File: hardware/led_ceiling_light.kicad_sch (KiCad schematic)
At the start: 22 parts

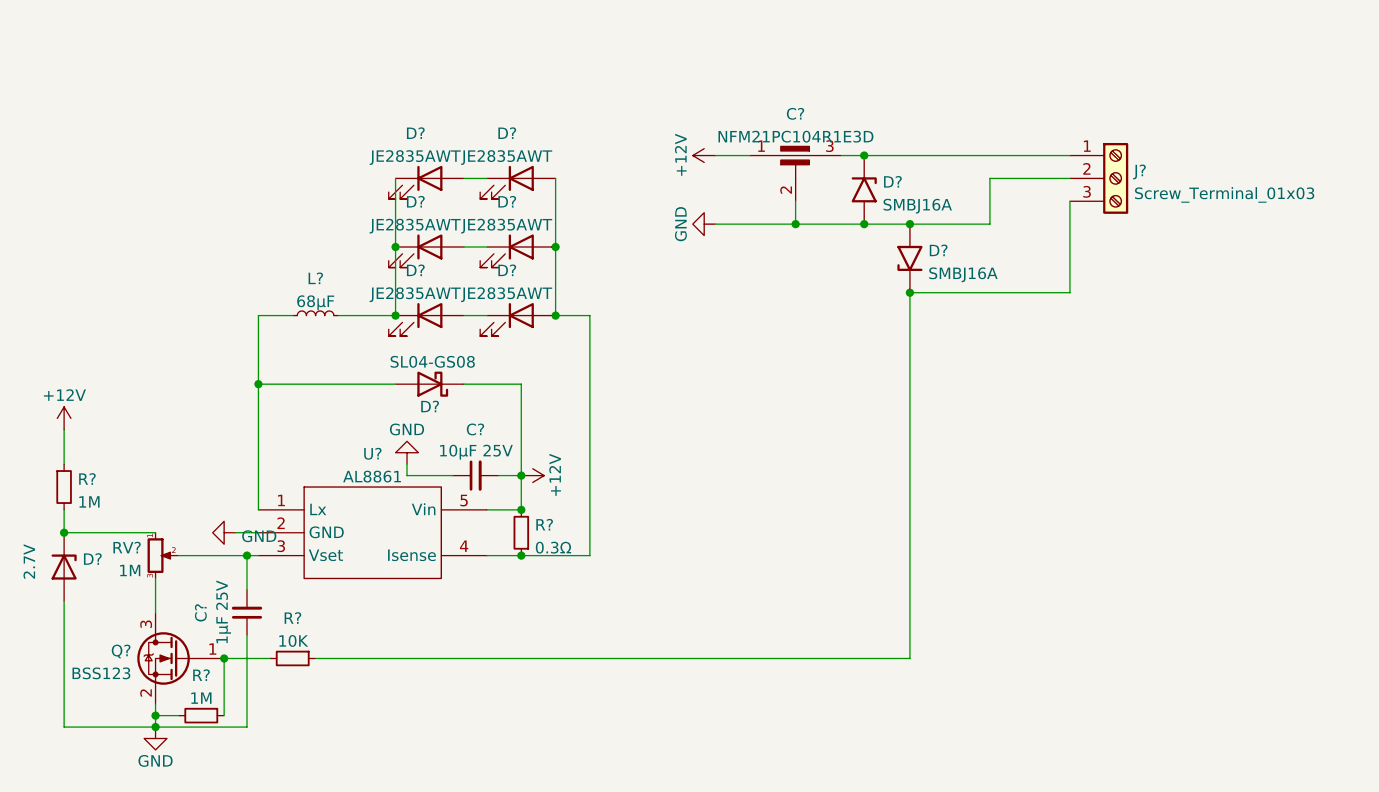
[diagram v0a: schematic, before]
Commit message: Fix some DRC issues; add more footprints.
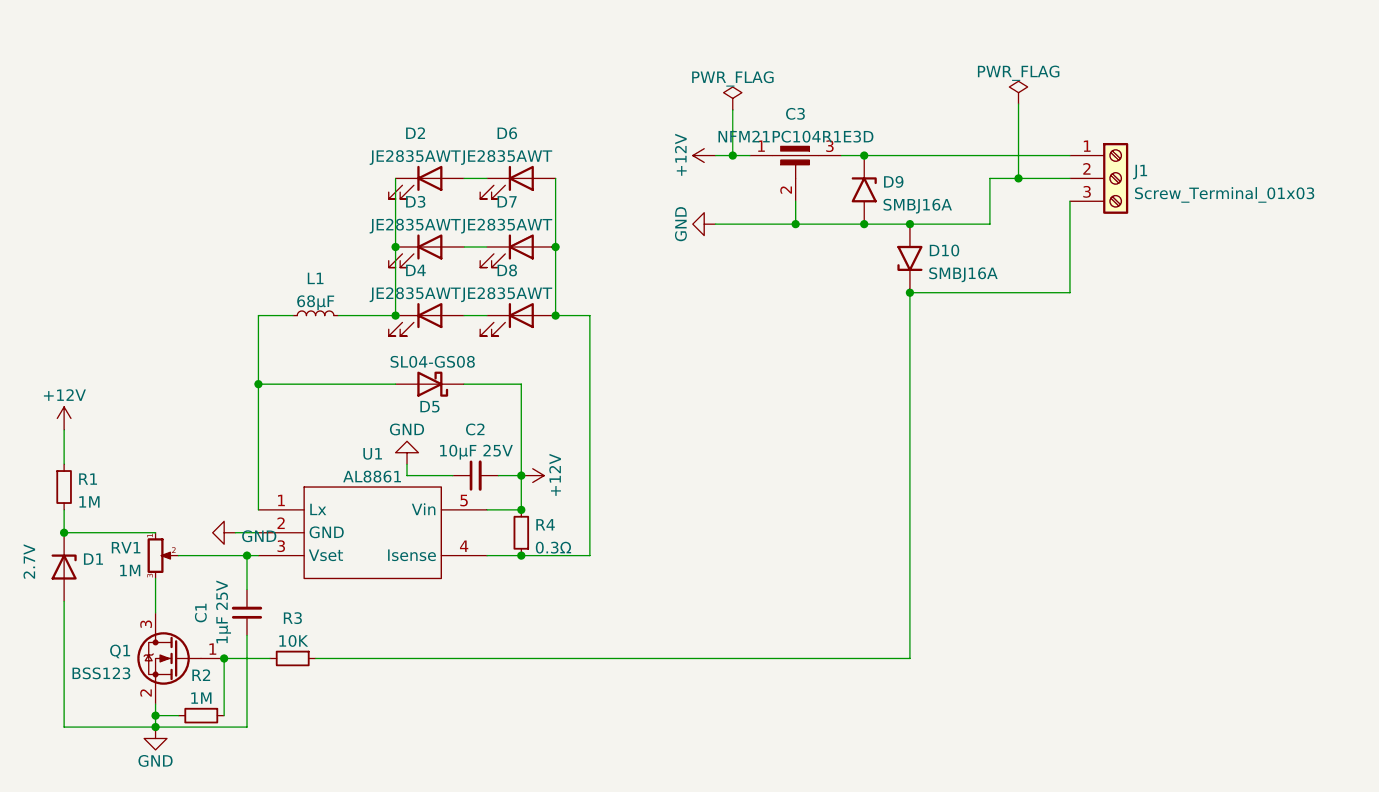
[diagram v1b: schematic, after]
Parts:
- Q1: renamed from Q?; footprint (none) -> Package_TO_SOT_SMD:SOT-23
- gave numbers to parts that had none: 21

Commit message: More part numbers and footprint
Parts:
- R1: footprint Resistor_SMD:R_0805_2012Metric_Pad1.20x1.40mm_HandSolder -> Resistor_SMD:R_2512_6332Metric_Pad1.40x3.35mm_HandSolder; P/N (none) -> WW25WR300FTL
- RV1: footprint (none) -> Potentiometer_THT:Potentiometer_Piher_PT-10-V10_Vertical; P/N (none) -> pt10lv10-105a2020-s
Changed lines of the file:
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@@
       (effects (font (size 1.27 1.27)) (justify right))
     )
-    (property "Footprint" "" (id 2) (at 110.49 99.06 0)
+    (property "Footprint" "Potentiometer_THT:Potentiometer_Piher_PT-10-V10_Vertical" (id 2) (at 110.49 99.06 0)
       (effects (font (size 1.27 1.27)) hide)
     )
     (property "Datasheet" "~" (id 3) (at 110.49 99.06 0)
+      (effects (font (size 1.27 1.27)) hide)
+    )
+    (property "P/N" "pt10lv10-105a2020-s" (id 4) (at 110.49 99.06 0)
       (effects (font (size 1.27 1.27)) hide)
     )
@@
       (effects (font (size 1.27 1.27)) (justify left))
     )
-    (property "Footprint" "Resistor_SMD:R_0805_2012Metric_Pad1.20x1.40mm_HandSolder" (id 2) (at 100.33 91.44 0)
+    (property "Footprint" "Resistor_SMD:R_2512_6332Metric_Pad1.40x3.35mm_HandSolder" (id 2) (at 100.33 91.44 0)
       (effects (font (size 1.27 1.27)) hide)
     )
     (property "Datasheet" "~" (id 3) (at 100.33 91.44 0)
+      (effects (font (size 1.27 1.27)) hide)
+    )
+    (property "P/N" " WW25WR300FTL " (id 4) (at 100.33 91.44 0)
       (effects (font (size 1.27 1.27)) hide)
     )
@@
     )
     (path "/7fd0a2b4-542e-44c7-acbf-294bb4a0590c"
-      (reference "R1") (unit 1) (value "1M") (footprint "Resistor_SMD:R_0805_2012Metric_Pad1.20x1.40mm_HandSolder")
+      (reference "R1") (unit 1) (value "1M") (footprint "Resistor_SMD:R_2512_6332Metric_Pad1.40x3.35mm_HandSolder")
     )
     (path "/c7222b6a-06a9-4042-b6f2-a18043608bdc"
@@
     )
     (path "/512ed214-cf7d-40c8-a2e8-0df6919047f4"
-      (reference "RV1") (unit 1) (value "1M") (footprint "")
+      (reference "RV1") (unit 1) (value "1M") (footprint "Potentiometer_THT:Potentiometer_Piher_PT-10-V10_Vertical")
     )
     (path "/b09ac753-e1cb-48a2-a548-b47dc09b2ff9"

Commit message: One last P/N
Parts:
- R2: value 1M -> 976K; footprint Resistor_SMD:R_0805_2012Metric_Pad1.20x1.40mm_HandSolder -> Resistor_SMD:R_0603_1608Metric_Pad0.98x0.95mm_HandSolder; P/N (none) -> stock
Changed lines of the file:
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@@
     (in_bom yes) (on_board yes) (fields_autoplaced)
     (property "Reference" "R2" (id 0) (at 115.57 112.4036 90))
-    (property "Value" "1M" (id 1) (at 115.57 114.9405 90))
-    (property "Footprint" "Resistor_SMD:R_0805_2012Metric_Pad1.20x1.40mm_HandSolder" (id 2) (at 115.57 116.84 0)
+    (property "Value" "976K" (id 1) (at 115.57 114.9405 90))
+    (property "Footprint" "Resistor_SMD:R_0603_1608Metric_Pad0.98x0.95mm_HandSolder" (id 2) (at 115.57 116.84 0)
       (effects (font (size 1.27 1.27)) hide)
     )
     (property "Datasheet" "~" (id 3) (at 115.57 116.84 0)
+      (effects (font (size 1.27 1.27)) hide)
+    )
+    (property "P/N" "stock" (id 4) (at 115.57 116.84 90)
       (effects (font (size 1.27 1.27)) hide)
     )
@@
     )
     (path "/c7222b6a-06a9-4042-b6f2-a18043608bdc"
-      (reference "R2") (unit 1) (value "1M") (footprint "Resistor_SMD:R_0805_2012Metric_Pad1.20x1.40mm_HandSolder")
+      (reference "R2") (unit 1) (value "976K") (footprint "Resistor_SMD:R_0603_1608Metric_Pad0.98x0.95mm_HandSolder")
     )
     (path "/db6af3bf-0a13-458a-b869-18de461e6f04"

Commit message: complete P/N and footprints
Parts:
- J1: footprint (none) -> TerminalBlock_TE-Connectivity:TerminalBlock_TE_282834-3_1x03_P2.54mm_Horizontal; P/N (none) -> 282834-3 (stock)
- R1: value 1M -> 976k; footprint Resistor_SMD:R_2512_6332Metric_Pad1.40x3.35mm_HandSolder -> Resistor_SMD:R_0603_1608Metric_Pad0.98x0.95mm_HandSolder; P/N WW25WR300FTL -> (none)
- R4: footprint (none) -> Resistor_SMD:R_1206_3216Metric_Pad1.30x1.75mm_HandSolder; P/N (none) -> MFHA1206R3000FC
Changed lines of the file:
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@@
       (effects (font (size 1.27 1.27)) (justify right))
     )
-    (property "Footprint" "" (id 2) (at 151.13 96.52 0)
+    (property "Footprint" "Resistor_SMD:R_1206_3216Metric_Pad1.30x1.75mm_HandSolder" (id 2) (at 151.13 96.52 0)
       (effects (font (size 1.27 1.27)) hide)
     )
     (property "Datasheet" "~" (id 3) (at 151.13 96.52 0)
+      (effects (font (size 1.27 1.27)) hide)
+    )
+    (property "P/N" " MFHA1206R3000FC " (id 4) (at 151.13 96.52 0)
       (effects (font (size 1.27 1.27)) hide)
     )
@@
       (effects (font (size 1.27 1.27)) (justify left))
     )
-    (property "Value" "1M" (id 1) (at 101.8286 93.1422 0)
-      (effects (font (size 1.27 1.27)) (justify left))
-    )
-    (property "Footprint" "Resistor_SMD:R_2512_6332Metric_Pad1.40x3.35mm_HandSolder" (id 2) (at 100.33 91.44 0)
+    (property "Value" "976k" (id 1) (at 101.8286 93.1422 0)
+      (effects (font (size 1.27 1.27)) (justify left))
+    )
+    (property "Footprint" "Resistor_SMD:R_0603_1608Metric_Pad0.98x0.95mm_HandSolder" (id 2) (at 100.33 91.44 0)
       (effects (font (size 1.27 1.27)) hide)
     )
     (property "Datasheet" "~" (id 3) (at 100.33 91.44 0)
-      (effects (font (size 1.27 1.27)) hide)
-    )
-    (property "P/N" " WW25WR300FTL " (id 4) (at 100.33 91.44 0)
       (effects (font (size 1.27 1.27)) hide)
     )
@@
       (effects (font (size 1.27 1.27)) (justify left))
     )
-    (property "Footprint" "" (id 2) (at 217.17 57.15 0)
+    (property "Footprint" "TerminalBlock_TE-Connectivity:TerminalBlock_TE_282834-3_1x03_P2.54mm_Horizontal" (id 2) (at 217.17 57.15 0)
       (effects (font (size 1.27 1.27)) hide)
     )
     (property "Datasheet" "~" (id 3) (at 217.17 57.15 0)
+      (effects (font (size 1.27 1.27)) hide)
+    )
+    (property "P/N" "282834-3 (stock)" (id 4) (at 217.17 57.15 0)
       (effects (font (size 1.27 1.27)) hide)
     )
@@
     )
     (path "/bf06e978-418f-42d7-bbde-c8a97f9d162c"
-      (reference "J1") (unit 1) (value "Screw_Terminal_01x03") (footprint "")
+      (reference "J1") (unit 1) (value "Screw_Terminal_01x03") (footprint "TerminalBlock_TE-Connectivity:TerminalBlock_TE_282834-3_1x03_P2.54mm_Horizontal")
     )
     (path "/52194c94-e7df-49ff-beb1-04a1b4f2344e"
@@
     )
     (path "/7fd0a2b4-542e-44c7-acbf-294bb4a0590c"
-      (reference "R1") (unit 1) (value "1M") (footprint "Resistor_SMD:R_2512_6332Metric_Pad1.40x3.35mm_HandSolder")
+      (reference "R1") (unit 1) (value "976k") (footprint "Resistor_SMD:R_0603_1608Metric_Pad0.98x0.95mm_HandSolder")
     )
     (path "/c7222b6a-06a9-4042-b6f2-a18043608bdc"
@@
     )
     (path "/126dd70c-c472-4281-967c-291d3e8d19db"
-      (reference "R4") (unit 1) (value "0.3Ω") (footprint "")
+      (reference "R4") (unit 1) (value "0.3Ω") (footprint "Resistor_SMD:R_1206_3216Metric_Pad1.30x1.75mm_HandSolder")
     )
     (path "/512ed214-cf7d-40c8-a2e8-0df6919047f4"

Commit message: Dedup resistor value
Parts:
- R1: value 976k -> 976K
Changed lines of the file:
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@@
       (effects (font (size 1.27 1.27)) (justify left))
     )
-    (property "Value" "976k" (id 1) (at 101.8286 93.1422 0)
+    (property "Value" "976K" (id 1) (at 101.8286 93.1422 0)
       (effects (font (size 1.27 1.27)) (justify left))
     )
@@
     )
     (path "/7fd0a2b4-542e-44c7-acbf-294bb4a0590c"
-      (reference "R1") (unit 1) (value "976k") (footprint "Resistor_SMD:R_0603_1608Metric_Pad0.98x0.95mm_HandSolder")
+      (reference "R1") (unit 1) (value "976K") (footprint "Resistor_SMD:R_0603_1608Metric_Pad0.98x0.95mm_HandSolder")
     )
     (path "/c7222b6a-06a9-4042-b6f2-a18043608bdc"

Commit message: normalise and update P/N, update footprint to match
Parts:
- C1: P/N (none) -> 08053C105KAT9A (stock)
- C2: value 10µF 25V -> 10µF25V; P/N (none) -> GCM32ER71E106KA57L (stock)
- C3: value NFM21PC104R1E3D -> 100n
- D5: P/N SL04-GS08 -> SL04-GS08 (stock)
- L1: value 68µF -> 68µH
- Q1: P/N BSS123 -> BSS123 (stock)
- R1, R3: P/N (none) -> stock
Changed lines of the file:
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@@
     (in_bom yes) (on_board yes)
     (property "Reference" "C2" (id 0) (at 146.05 85.09 90))
-    (property "Value" "10µF 25V" (id 1) (at 146.0563 87.445 90))
+    (property "Value" "10µF25V" (id 1) (at 146.0563 87.445 90))
     (property "Footprint" "Capacitor_SMD:C_1210_3225Metric_Pad1.33x2.70mm_HandSolder" (id 2) (at 146.05 90.17 0)
       (effects (font (size 1.27 1.27)) hide)
     )
     (property "Datasheet" "~" (id 3) (at 146.05 90.17 0)
+      (effects (font (size 1.27 1.27)) hide)
+    )
+    (property "P/N" "GCM32ER71E106KA57L (stock)" (id 4) (at 146.05 90.17 0)
       (effects (font (size 1.27 1.27)) hide)
     )
@@
     (in_bom yes) (on_board yes) (fields_autoplaced)
     (property "Reference" "L1" (id 0) (at 128.27 68.3092 90))
-    (property "Value" "68µF" (id 1) (at 128.27 70.8461 90))
+    (property "Value" "68µH" (id 1) (at 128.27 70.8461 90))
     (property "Footprint" "Inductor_SMD:L_Taiyo-Yuden_NR-80xx_HandSoldering" (id 2) (at 128.27 72.39 0)
       (effects (font (size 1.27 1.27)) hide)
@@
       (effects (font (size 1.27 1.27)) hide)
     )
+    (property "P/N" "08053C105KAT9A (stock)" (id 4) (at 120.65 105.41 0)
+      (effects (font (size 1.27 1.27)) hide)
+    )
     (pin "1")
     (pin "2")
@@
       (effects (font (size 1.27 1.27)) hide)
     )
+    (property "P/N" "stock" (id 4) (at 100.33 91.44 0)
+      (effects (font (size 1.27 1.27)) hide)
+    )
     (pin "1")
     (pin "2")
@@
       (effects (font (size 1.27 1.27)) hide)
     )
-    (property "P/N" "BSS123" (id 4) (at 113.03 110.49 0)
+    (property "P/N" "BSS123 (stock)" (id 4) (at 113.03 110.49 0)
       (effects (font (size 1.27 1.27)) hide)
     )
@@
       (effects (font (size 1.27 1.27)) hide)
     )
-    (property "P/N" "SL04-GS08" (id 4) (at 140.97 80.01 0)
+    (property "P/N" "SL04-GS08 (stock)" (id 4) (at 140.97 80.01 0)
       (effects (font (size 1.27 1.27)) hide)
     )
@@
       (effects (font (size 1.27 1.27)) hide)
     )
+    (property "P/N" "stock" (id 4) (at 125.73 110.49 0)
+      (effects (font (size 1.27 1.27)) hide)
+    )
     (pin "1")
     (pin "2")
@@
     (in_bom yes) (on_board yes) (fields_autoplaced)
     (property "Reference" "C3" (id 0) (at 181.61 50.0212 0))
-    (property "Value" "NFM21PC104R1E3D " (id 1) (at 181.61 52.5581 0))
+    (property "Value" "100n" (id 1) (at 181.61 52.5581 0))
     (property "Footprint" "local:C_filter_0805" (id 2) (at 181.61 57.15 90)
       (effects (font (size 1.27 1.27)) hide)
@@
     )
     (path "/2a77a72e-d058-40b9-a6e8-cfe4c97e7ab1"
-      (reference "C2") (unit 1) (value "10µF 25V") (footprint "Capacitor_SMD:C_1210_3225Metric_Pad1.33x2.70mm_HandSolder")
+      (reference "C2") (unit 1) (value "10µF25V") (footprint "Capacitor_SMD:C_1210_3225Metric_Pad1.33x2.70mm_HandSolder")
     )
     (path "/f60a8a1b-d446-41d2-a04c-d3d1dc2abea6"
-      (reference "C3") (unit 1) (value "NFM21PC104R1E3D ") (footprint "local:C_filter_0805")
+      (reference "C3") (unit 1) (value "100n") (footprint "local:C_filter_0805")
     )
     (path "/591c7a48-6647-47f5-be47-c2508213f188"
@@
     )
     (path "/52194c94-e7df-49ff-beb1-04a1b4f2344e"
-      (reference "L1") (unit 1) (value "68µF") (footprint "Inductor_SMD:L_Taiyo-Yuden_NR-80xx_HandSoldering")
+      (reference "L1") (unit 1) (value "68µH") (footprint "Inductor_SMD:L_Taiyo-Yuden_NR-80xx_HandSoldering")
     )
     (path "/a2b9108e-8d68-4bc9-996e-d8350a16fdeb"

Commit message: Final pass on part numbers
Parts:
- C3: P/N NFM21PC104R1E3D -> NFM21PC104R1E3D (M)
- D1: P/N ZMM5223B 2.7V -> ZMM5223B (M)
- D10, D9: P/N SMBJ16A -> SMBJ16Ae3/TR13 (M)
- D2, D3, D4, D6, D7, D8: P/N JE2835AWT-00-0000-000A0HG940E -> JE2835AWT-00-0000-000A0HG940E (stock)
- L1: P/N NR8040T680M -> NR8040T680M (M)
- R4: P/N MFHA1206R3000FC -> MFHA1206R3000FC (M)
- RV1: P/N pt10lv10-105a2020-s -> pt10lv10-105a2020-s (F)
- U1: P/N AL8861WT-7 -> AL8861WT-7 (M)
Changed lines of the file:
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@@
       (effects (font (size 1.27 1.27)) hide)
     )
-    (property "P/N" " MFHA1206R3000FC " (id 4) (at 151.13 96.52 0)
+    (property "P/N" "MFHA1206R3000FC (M)" (id 4) (at 151.13 96.52 0)
       (effects (font (size 1.27 1.27)) hide)
     )
@@
       (effects (font (size 1.27 1.27)) hide)
     )
-    (property "P/N" "pt10lv10-105a2020-s" (id 4) (at 110.49 99.06 0)
+    (property "P/N" "pt10lv10-105a2020-s (F)" (id 4) (at 110.49 99.06 0)
       (effects (font (size 1.27 1.27)) hide)
     )
@@
       (effects (font (size 1.27 1.27)) hide)
     )
-    (property "P/N" "NR8040T680M" (id 4) (at 128.27 72.39 90)
+    (property "P/N" "NR8040T680M (M)" (id 4) (at 128.27 72.39 90)
       (effects (font (size 1.27 1.27)) hide)
     )
@@
       (effects (font (size 1.27 1.27)) hide)
     )
-    (property "P/N" " ZMM5223B  2.7V" (id 4) (at 100.33 100.33 90)
+    (property "P/N" " ZMM5223B (M)" (id 4) (at 100.33 100.33 90)
       (effects (font (size 1.27 1.27)) hide)
     )
@@
       (effects (font (size 1.27 1.27)) hide)
     )
-    (property "P/N" "JE2835AWT-00-0000-000A0HG940E" (id 4) (at 151.13 57.15 0)
+    (property "P/N" "JE2835AWT-00-0000-000A0HG940E (stock)" (id 4) (at 151.13 57.15 0)
       (effects (font (size 1.27 1.27)) hide)
     )
@@
       (effects (font (size 1.27 1.27)) hide)
     )
-    (property "P/N" "JE2835AWT-00-0000-000A0HG940E" (id 4) (at 140.97 57.15 0)
+    (property "P/N" "JE2835AWT-00-0000-000A0HG940E (stock)" (id 4) (at 140.97 57.15 0)
       (effects (font (size 1.27 1.27)) hide)
     )
@@
       (effects (font (size 1.27 1.27)) hide)
     )
-    (property "P/N" "JE2835AWT-00-0000-000A0HG940E" (id 4) (at 151.13 72.39 0)
+    (property "P/N" "JE2835AWT-00-0000-000A0HG940E (stock)" (id 4) (at 151.13 72.39 0)
       (effects (font (size 1.27 1.27)) hide)
     )
@@
       (effects (font (size 1.27 1.27)) hide)
     )
-    (property "P/N" "SMBJ16A" (id 4) (at 189.23 58.42 90)
+    (property "P/N" " SMBJ16Ae3/TR13 (M)" (id 4) (at 189.23 58.42 90)
       (effects (font (size 1.27 1.27)) hide)
     )
@@
       (effects (font (size 1.27 1.27)) hide)
     )
-    (property "P/N" "AL8861WT-7" (id 4) (at 134.62 96.52 0)
+    (property "P/N" "AL8861WT-7 (M)" (id 4) (at 134.62 96.52 0)
       (effects (font (size 1.27 1.27)) hide)
     )
@@
       (effects (font (size 1.27 1.27)) hide)
     )
-    (property "P/N" "SMBJ16A" (id 4) (at 194.31 66.04 90)
+    (property "P/N" " SMBJ16Ae3/TR13 (M)" (id 4) (at 194.31 66.04 90)
       (effects (font (size 1.27 1.27)) hide)
     )
@@
       (effects (font (size 1.27 1.27)) hide)
     )
-    (property "P/N" "JE2835AWT-00-0000-000A0HG940E" (id 4) (at 140.97 72.39 0)
+    (property "P/N" "JE2835AWT-00-0000-000A0HG940E (stock)" (id 4) (at 140.97 72.39 0)
       (effects (font (size 1.27 1.27)) hide)
     )
@@
       (effects (font (size 1.27 1.27)) hide)
     )
-    (property "P/N" "JE2835AWT-00-0000-000A0HG940E" (id 4) (at 140.97 64.77 0)
+    (property "P/N" "JE2835AWT-00-0000-000A0HG940E (stock)" (id 4) (at 140.97 64.77 0)
       (effects (font (size 1.27 1.27)) hide)
     )
@@
       (effects (font (size 1.27 1.27)) hide)
     )
-    (property "P/N" "JE2835AWT-00-0000-000A0HG940E" (id 4) (at 151.13 64.77 0)
+    (property "P/N" "JE2835AWT-00-0000-000A0HG940E (stock)" (id 4) (at 151.13 64.77 0)
       (effects (font (size 1.27 1.27)) hide)
     )
@@
       (effects (font (size 1.27 1.27)) hide)
     )
-    (property "P/N" "NFM21PC104R1E3D " (id 4) (at 181.61 57.15 0)
-      (effects (font (size 1.27 1.27)) hide)
-    )
+    (property "P/N" "NFM21PC104R1E3D (M)" (id 4) (at 181.61 57.15 0)
+      (effects (font (size 1.27 1.27)) hide)
+    )
